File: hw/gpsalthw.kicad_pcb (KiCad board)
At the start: 2 copper layers, 54.9 x 55.4 mm, 48 parts, among them J1 serial, J2 display, J3 antenna, J4 USB_B_Micro, J5 battery, Q1 IRLML5203TRPBF, Q2 IRLML5203TRPBF, SW1 reset, SW2 boot, SW3 btn-up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

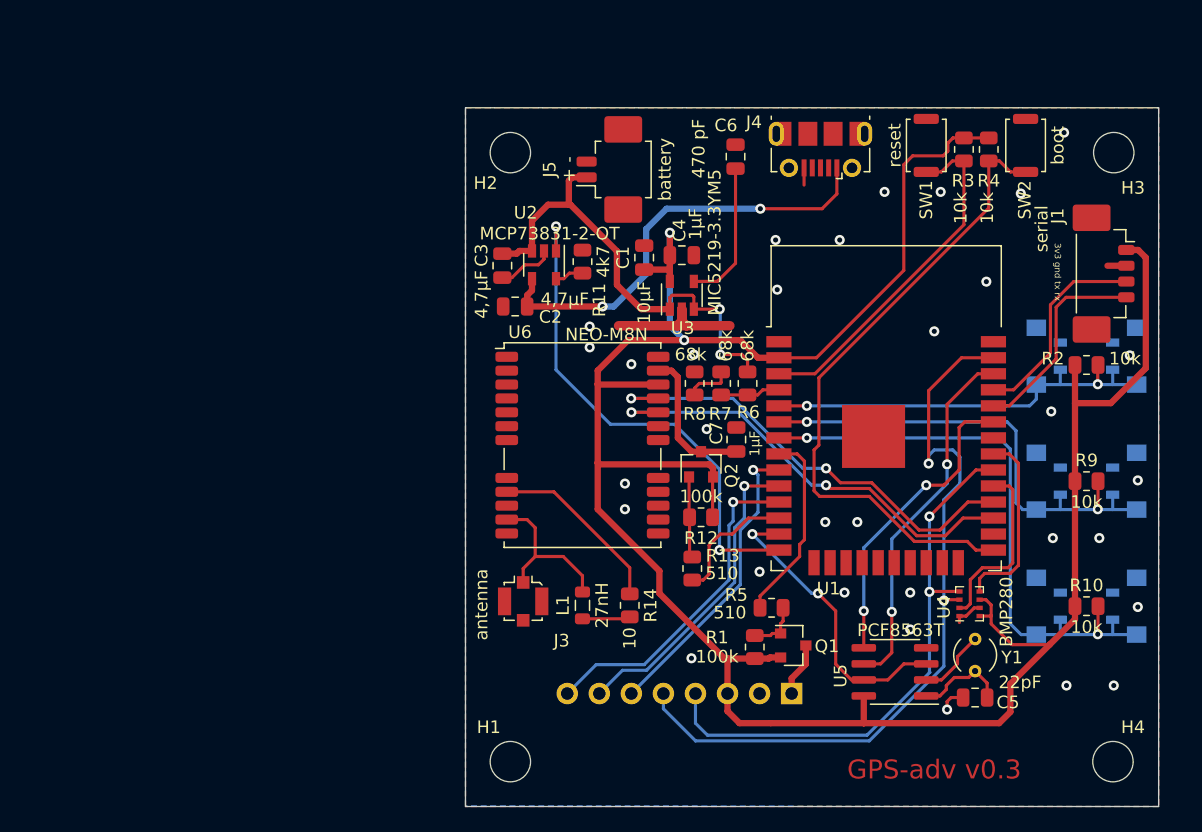
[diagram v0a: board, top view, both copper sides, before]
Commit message: плата - контур платы, отверстия, примерно раскиданы элементы
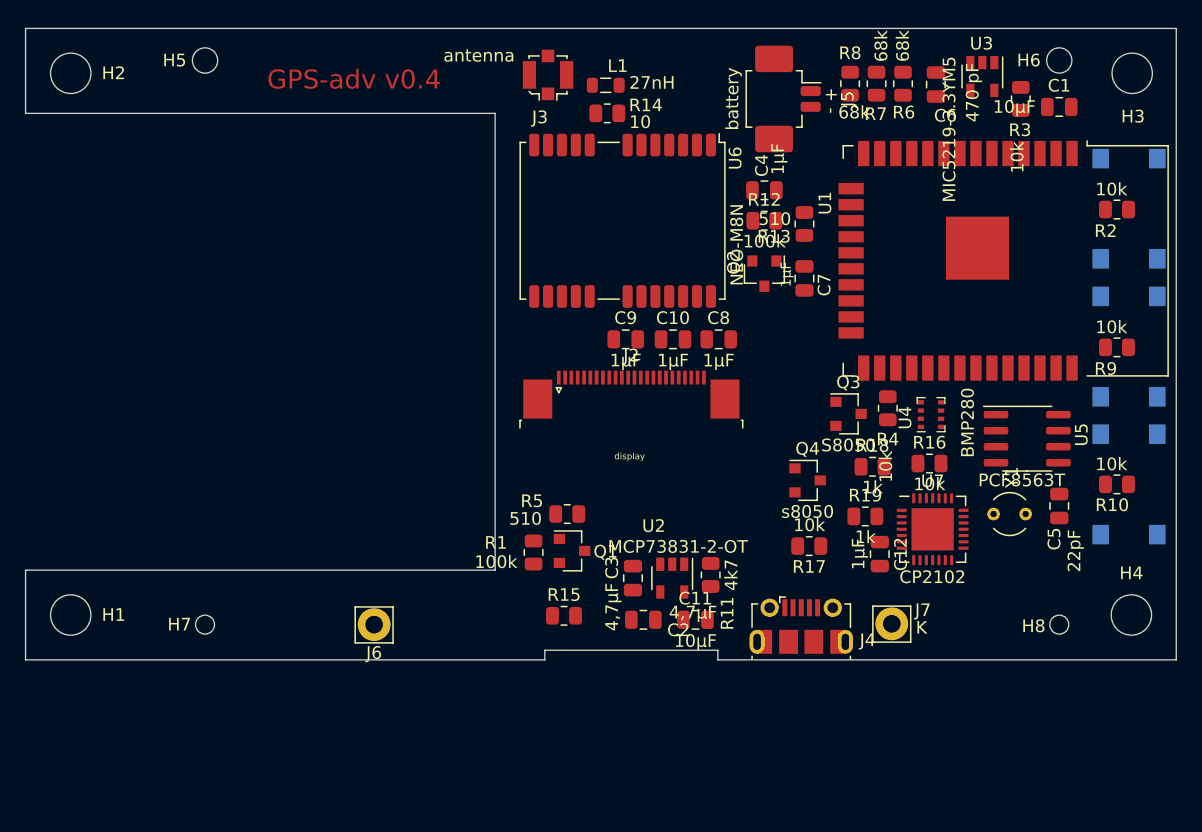
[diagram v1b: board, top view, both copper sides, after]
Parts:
- removed J1: serial, Connector_Molex:Molex_PicoBlade_53398-0471_1x04-1MP_P1.25mm_Vertical
- removed SW1: reset, Button_Switch_SMD:SW_Push_SPST_NO_Alps_SKRK
- removed SW2: boot, Button_Switch_SMD:SW_Push_SPST_NO_Alps_SKRK
- removed SW6: btn-up2, Button_Switch_SMD:SW_Push_1P1T_NO_6x6mm_H9.5mm
- removed SW7: btn-sel2, Button_Switch_SMD:SW_Push_1P1T_NO_6x6mm_H9.5mm
- removed SW8: btn-down2, Button_Switch_SMD:SW_Push_1P1T_NO_6x6mm_H9.5mm
- added C10: 1μF, Capacitor_SMD:C_0805_2012Metric, F.Cu at (96.1, 61.5)
- added C11: 10μF, Capacitor_SMD:C_0805_2012Metric, F.Cu at (97.9, 83.7)
- added C12: 1μF, Capacitor_SMD:C_0805_2012Metric, F.Cu at (112.5, 78.5)
- added C8: 1μF, Capacitor_SMD:C_0805_2012Metric, F.Cu at (99.8, 61.5)
- added C9: 1μF, Capacitor_SMD:C_0805_2012Metric, F.Cu at (92.4, 61.5)
- added H5: MountingHole, MHole:MountingHole_2.0, F.Cu at (59.1, 39.4)
- added H6: MountingHole, MHole:MountingHole_2.0, F.Cu at (126.7, 39.4)
- added H7: MountingHole, MHole:MountingHole_1.5, F.Cu at (59.1, 84.1)
- added H8: MountingHole, MHole:MountingHole_1.5, F.Cu at (126.7, 84.1)
- added J6: A, Connector_Pin:Pin_D1.4mm_L8.5mm_W2.8mm_FlatFork, F.Cu at (72.5, 84.1)
- added J7: K, Connector_Pin:Pin_D1.4mm_L8.5mm_W2.8mm_FlatFork, F.Cu at (113.5, 84.0)
- added Q3: S8050, Package_TO_SOT_SMD:SOT-23, F.Cu at (110.0, 67.4)
- added Q4: s8050, Package_TO_SOT_SMD:SOT-23, F.Cu at (106.8, 72.6)
- added R15: 510, Resistor_SMD:R_0805_2012Metric, F.Cu at (87.5, 83.4)
- added R16: 10k, Resistor_SMD:R_0805_2012Metric, F.Cu at (116.5, 71.3)
- added R17: 10k, Resistor_SMD:R_0805_2012Metric, F.Cu at (106.9, 77.9)
- added R18: 1k, Resistor_SMD:R_0805_2012Metric, F.Cu at (112.0, 71.6)
- added R19: 1k, Resistor_SMD:R_0805_2012Metric, F.Cu at (111.4, 75.5)
- added U7: CP2102, Package_DFN_QFN:QFN-28-1EP_5x5mm_P0.5mm_EP3.35x3.35mm, F.Cu at (116.7, 76.5)
- J2: footprint Connector_PinHeader_2.54mm:PinHeader_1x08_P2.54mm_Vertical -> Connector_FFC-FPC:TE_2-1734839-4_1x24-1MP_P0.5mm_Horizontal; moved to F.Cu
- SW3, SW4, SW5: footprint Button_Switch_SMD:SW_SPST_PTS810 -> Button_Switch_SMD:SW_Push_1P1T_NO_6x6mm_H9.5mm
- moved J3 41.8 mm to (86.2, 40.5), turned to 0 degrees
- moved L1 41.3 mm to (90.8, 41.3), turned to 180 degrees
- moved R14 39.0 mm to (90.9, 43.6), turned to 0 degrees
- moved J4 37.8 mm to (106.3, 84.2), turned to 0 degrees
- moved H1 36.7 mm to (48.4, 83.3)
- moved H2 35.4 mm to (48.4, 40.4)
- moved C1 35.0 mm to (126.7, 43.1), turned to 0 degrees
- moved U3 29.5 mm to (120.7, 40.6), turned to 270 degrees
- moved R13 28.7 mm to (106.6, 52.3), turned to 270 degrees
- moved J2 26.9 mm to (92.8, 65.8), turned to 0 degrees
- moved C3 26.8 mm to (93.0, 80.4)
- moved U2 26.8 mm to (96.1, 80.4)
- moved C2 26.8 mm to (93.8, 83.7)
- moved R11 26.8 mm to (99.1, 80.1)
- moved R6 26.8 mm to (114.4, 41.2)
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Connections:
- net /d-led renamed d-led
- net Net-(R3-Pad2) renamed /s-en
- net Net-(R4-Pad2) renamed /s-boot
- J2 pad 1: Net-(J2-Pad1) -> +3V3
- J2 pad 2: GND -> +3V3
- J2 pad 4: /spi-clk -> +3V3
- J2 pad 6: /d-rs-dc -> /spi-mosi
- J2 pad 7: /d-rst -> /spi-mosi
- J2 pad 8: /d-cs -> /spi-clk
- J4 pad 2: Net-(J4-Pad2) -> /usb-d-
- J4 pad 3: Net-(J4-Pad3) -> /usb-d+
- Q1 pad 3: Net-(J2-Pad1) -> Net-(Q1-Pad3)
- U1 pad 34: /RX -> /s-rx
- U1 pad 35: /TX -> /s-tx
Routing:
- net +3V3: track 194.7 -> 0.00 mm, vias 2 -> 0
- net /spi-mosi: track 60.8 -> 0.00 mm, vias 2 -> 0
- net /s-boot: track 51.3 -> 0.00 mm
- net /b-down: track 47.6 -> 0.00 mm, vias 2 -> 0
- net /spi-clk: track 44.7 -> 0.00 mm, vias 2 -> 0
- net chg-ind: track 40.7 -> 0.00 mm, vias 2 -> 0
- net /b-sel: track 39.2 -> 0.00 mm, vias 2 -> 0
- net +BATT: track 37.9 -> 0.00 mm, vias 2 -> 0
- net /gps-rx: track 36.1 -> 0.00 mm, vias 2 -> 0
- net /gps-tx: track 35.4 -> 0.00 mm, vias 2 -> 0
- net /usb-5v: track 34.6 -> 0.00 mm, vias 2 -> 0
- net /b-up: track 33.7 -> 0.00 mm, vias 2 -> 0
- net i2c-scl: track 28.8 -> 0.00 mm, vias 2 -> 0
- net /s-en: track 28.4 -> 0.00 mm
- net /d-cs: track 26.5 -> 0.00 mm, vias 1 -> 0
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- removed copper zone on B.Cu, net GND
- removed copper zone on F.Cu, net GND
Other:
- board size 54.9 x 55.4 mm -> 91.2 x 50 mm
- board text added: "GPS-adv v0.4"
- board text removed: "3v3 gnd tx rx"
- board text removed: "GPS-adv v0.3"
- board text removed: "led vss vdd sck sda dc rst cs"

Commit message: плата - расставлены компоненты выше разъёма дисплея (верхняя половина платы)
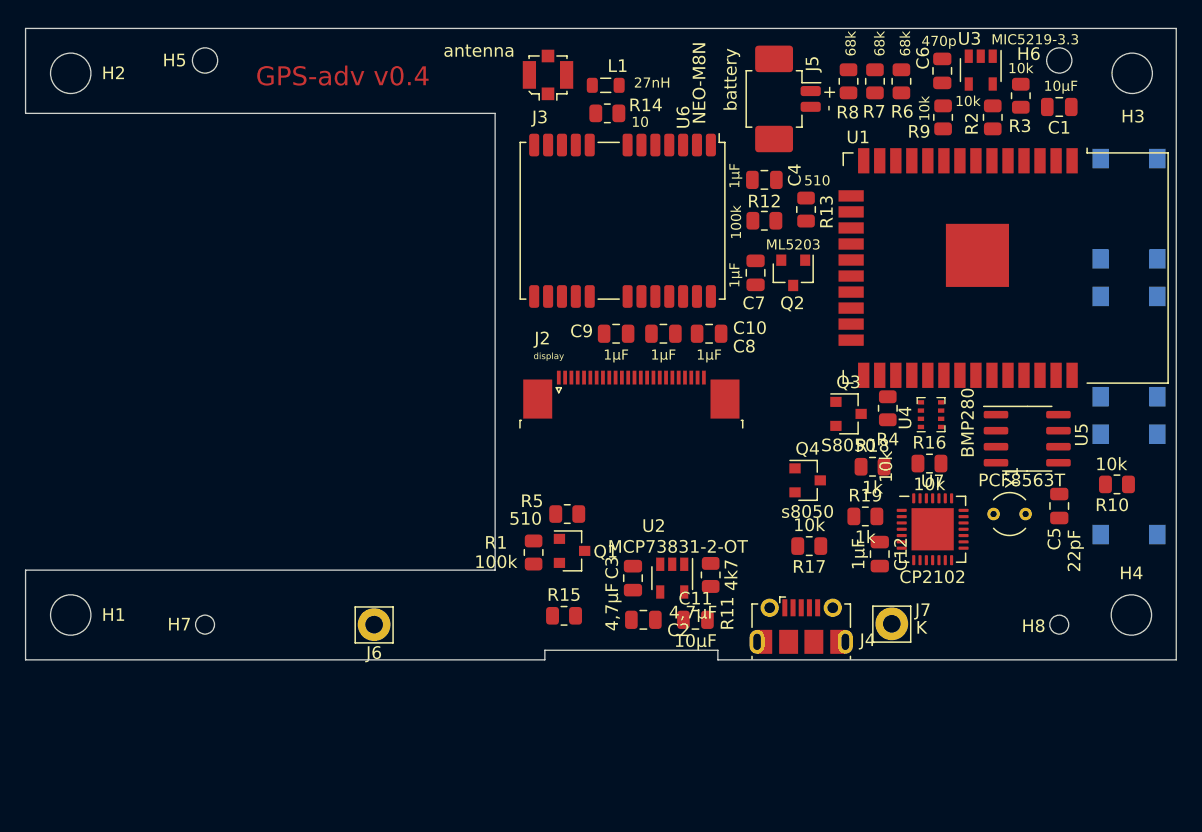
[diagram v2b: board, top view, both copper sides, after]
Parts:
- C6: value 470 pF -> 470p
- Q2: value IRLML5203TRPBF -> ML5203
- U3: value MIC5219-3.3YM5 -> MIC5219-3.3
- moved R9 22.8 mm to (117.5, 43.9), turned to 270 degrees
- moved R2 12.3 mm to (121.5, 43.9), turned to 270 degrees
- moved C7 3.90 mm to (102.7, 56.2)
- moved Q2 2.29 mm to (105.7, 56.2)
- moved C6 1.19 mm to (117.5, 40.2), turned to 90 degrees
- moved R13 1.15 mm to (106.7, 51.2)
- moved C10 0.88 mm to (95.4, 61.0)
- moved C8 0.88 mm to (99.0, 61.0)
- moved C9 0.88 mm to (91.6, 61.0)
- moved C4 0.83 mm to (103.4, 48.8)
- moved U1 0.57 mm to (119.5, 55.8)
- moved U3 0.52 mm to (120.5, 40.1)
- moved R3 0.25 mm to (123.7, 42.2)
- moved R6 0.23 mm to (114.2, 41.0)
- moved R7 0.23 mm to (112.1, 41.0)
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
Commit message: плата - скорректированы отверстия под дисплей
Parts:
- H5, H6: footprint MHole:MountingHole_2.0 -> MountingHole:MountingHole_2.2mm_M2
- J6, J7: footprint Connector_Pin:Pin_D1.4mm_L8.5mm_W2.8mm_FlatFork -> Connector_Wire:SolderWire-1sqmm_1x01_D1.4mm_OD2.7mm
- moved J7 0.20 mm to (113.3, 83.9)
- moved H6 0.14 mm to (126.9, 39.3)
- moved H5 0.14 mm to (58.9, 39.3)
- moved J6 0.14 mm to (72.5, 83.9)
- moved H8 0.13 mm to (126.9, 84.1)
- moved H7 0.13 mm to (58.9, 84.1)
